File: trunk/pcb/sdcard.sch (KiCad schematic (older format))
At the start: 17 parts, among them P1 SDC_MMC_SOCKET, P2 CONN_8, U1 DS1338-33, X1 32768

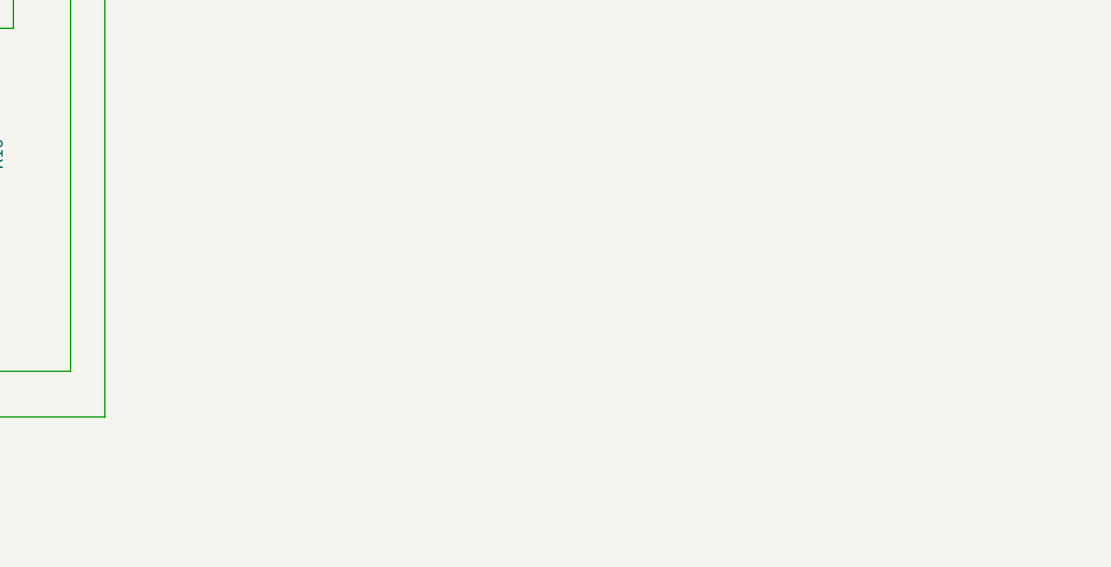
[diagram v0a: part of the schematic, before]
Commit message: Added SD card production files. (Didnt realise they werent already under version control.)
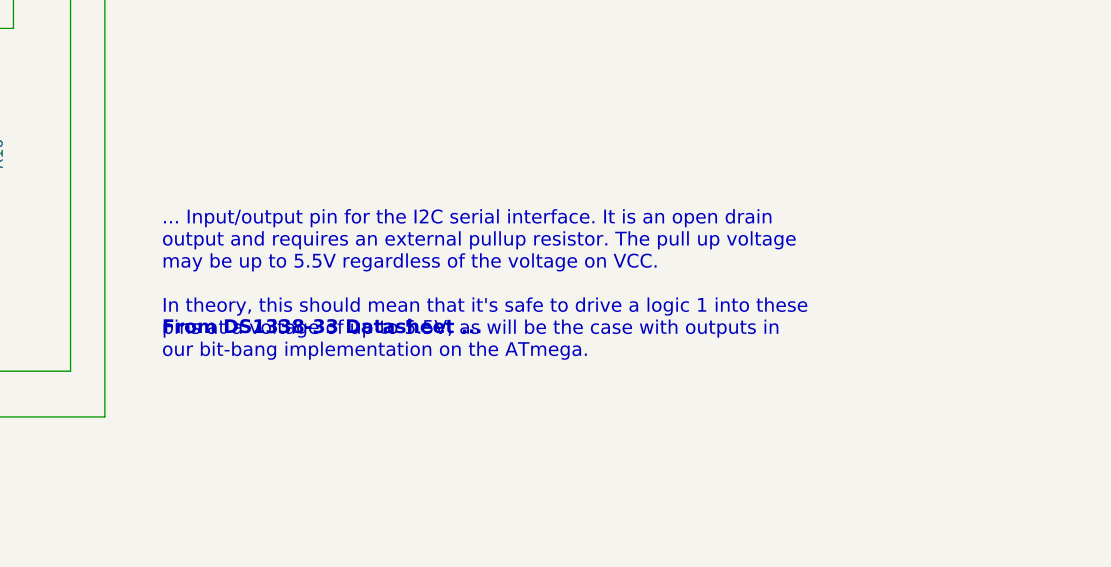
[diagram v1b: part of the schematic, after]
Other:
- note added: "... Input/output pin for the I2C serial interface. It is an open drain\noutput and requires an external pullup resistor. The pull up voltage\nmay be up to 5.5V regardless of the voltage on VCC.\n\nIn theory, this should mean that it's safe to drive a logic 1 into these\npins at a voltage of up to 5.5V, as will be the case with outputs in\nour bit-bang implementation on the ATmega."
- note added: "From DS1338-33 Datasheet ..."
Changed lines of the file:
@@
-EESchema Schematic File Version 2  date 14/02/2011 9:09:30 p.m.
+EESchema Schematic File Version 2  date 15/02/2011 9:38:49 p.m.
 LIBS:power
 LIBS:device
@@
 Sheet 1 1
 Title "sdcard.sch"
-Date "14 feb 2011"
+Date "15 feb 2011"
 Rev "3.3"
 Comp ""
@@
 Comment4 ""
 $EndDescr
+Text Notes 7400 4650 0    60   ~ 12
+From DS1338-33 Datasheet ...
+Text Notes 7400 4750 0    60   ~ 0
+... Input/output pin for the I2C serial interface. It is an open drain\noutput and requires an external pullup resistor. The pull up voltage\nmay be up to 5.5V regardless of the voltage on VCC.\n\nIn theory, this should mean that it's safe to drive a logic 1 into these\npins at a voltage of up to 5.5V, as will be the case with outputs in\nour bit-bang implementation on the ATmega.
 Connection ~ 4650 2650
 Wire Wire Line
